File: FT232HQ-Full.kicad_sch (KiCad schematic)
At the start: 29 parts, among them J1 USB_C_Receptacle_USB2.0_16P, J2 Conn_02x10_Odd_Even, J3 Conn_01x01, U4 12M, U5 FT232H, U6 93LCxxBxxOT

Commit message: update
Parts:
- J3: footprint 1st_commonly:hole -> 1st_commonly:NUT_SMD_M2.5_4.5_3.0
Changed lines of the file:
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@@
 			)
 		)
-		(property "Footprint" "1st_commonly:hole"
+		(property "Footprint" "1st_commonly:NUT_SMD_M2.5_4.5_3.0"
 			(at 220.98 95.25 0)
 			(effects

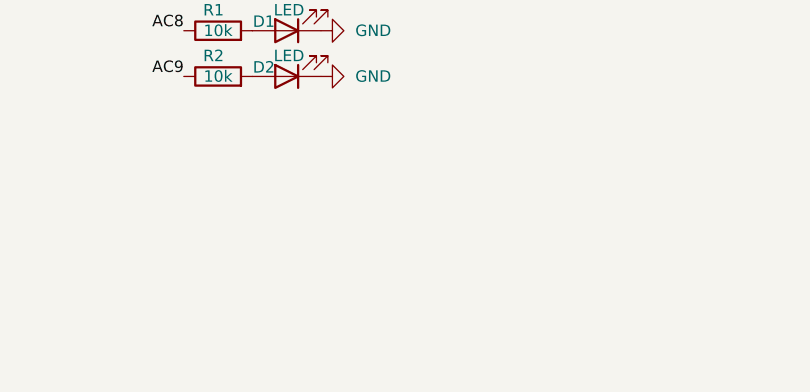
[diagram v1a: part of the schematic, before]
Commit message: add raspberrypi jst-sh1.0 uart
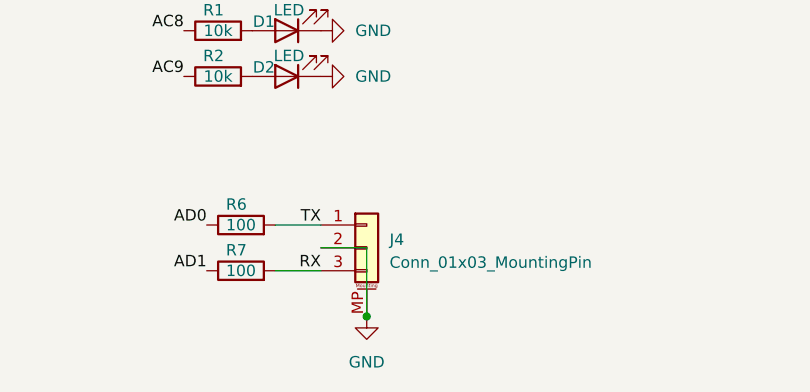
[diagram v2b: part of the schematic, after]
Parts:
- added J4: Conn_01x03_MountingPin, Connector_JST:JST_SH_SM03B-SRSS-TB_1x03-1MP_P1.00mm_Horizontal, symbol Connector_Generic_MountingPin:Conn_01x03_MountingPin
- added R6, R7: 100, Resistor_SMD:R_0402_1005Metric, symbol Device:R
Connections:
- net AD0: now also R6.1
- net AD1: now also R7.1
- net GND: now also J4.2 (Pin_2), J4.MP (MountPin)
- new net RX: J4.3 (Pin_3), R7.2
- new net TX: J4.1 (Pin_1), R6.2

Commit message: add 2.2uf to 5v
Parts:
- added C6: 225, Capacitor_SMD:C_0402_1005Metric, symbol Device:C
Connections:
- net +5V: now also C6.1
- net GND: now also C6.2
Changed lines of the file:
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@@
 	)
 	(junction
+		(at 41.91 97.79)
+		(diameter 0)
+		(color 0 0 0 0)
+	)
+	(junction
 		(at 262.89 68.58)
 		(diameter 0)
@@
 	)
 	(junction
+		(at 41.91 87.63)
+		(diameter 0)
+		(color 0 0 0 0)
+	)
+	(junction
 		(at 190.5 52.07)
 		(diameter 0)
@@
 	(wire
 		(pts
+			(xy 35.56 87.63) (xy 41.91 87.63)
+		)
+		(stroke
+			(width 0)
+			(type default)
+		)
+	)
+	(wire
+		(pts
 			(xy 189.23 64.77) (xy 201.93 64.77)
 		)
@@
 	(wire
 		(pts
+			(xy 35.56 97.79) (xy 41.91 97.79)
+		)
+		(stroke
+			(width 0)
+			(type default)
+		)
+	)
+	(wire
+		(pts
 			(xy 245.11 63.5) (xy 245.11 66.04)
 		)
@@
 	(wire
 		(pts
+			(xy 35.56 95.25) (xy 35.56 97.79)
+		)
+		(stroke
+			(width 0)
+			(type default)
+		)
+	)
+	(wire
+		(pts
 			(xy 262.89 71.12) (xy 262.89 68.58)
 		)
@@
 					(unit 1)
 				)
+			)
+		)
+	)
+	(symbol
+		(lib_id "Device:C")
+		(at 35.56 91.44 0)
+		(unit 1)
+		(exclude_from_sim no)
+		(in_bom yes)
+		(on_board yes)
+		(dnp no)
+		(fields_autoplaced yes)
+		(property "Reference" "C6"
+			(at 39.37 90.1699 0)
+			(effects
+				(font
+					(size 1.27 1.27)
+				)
+				(justify left)
+			)
+		)
+		(property "Value" "225"
+			(at 39.37 92.7099 0)
+			(effects
+				(font
+					(size 1.27 1.27)
+				)
+				(justify left)
+			)
+		)
+		(property "Footprint" "Capacitor_SMD:C_0402_1005Metric"
+			(at 36.5252 95.25 0)
+			(effects
+				(font
+					(size 1.27 1.27)
+				)
+				(hide yes)
+			)
+		)
+		(property "Datasheet" "~"
+			(at 35.56 91.44 0)
+			(effects
+				(font
+					(size 1.27 1.27)
+				)
+				(hide yes)
+			)
+		)
+		(property "Description" "Unpolarized capacitor"
+			(at 35.56 91.44 0)
+			(effects
+				(font
+					(size 1.27 1.27)
+				)
+				(hide yes)
+			)
+		)
+		(pin "2"
+		)
+		(pin "1"
+		)
+		(instances
+			(project "FT232HQ-Full"
+				(path "/dd4ac3e3-2410-4273-be8c-634c81d8b6b2"
+					(reference "C6")
+					(unit 1)
+				)
